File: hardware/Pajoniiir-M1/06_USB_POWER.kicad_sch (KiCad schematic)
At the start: 19 parts

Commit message: hardware: fix local symbol cache keys for ERC
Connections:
- net 5V_SYS: now also U_USB0.4 (EN), U_USB1.4 (EN)
- net GND: now also U_USB0.5 (GND), U_USB1.5 (GND)
- net USB0_FAULT_N: now also U_USB0.1 (OUT)
- net USB0_PWR_EN: now also U_USB0.6 (IN)
- net USB0_SW_OUT: now also U_USB0.3 (FAULT)
- net USB1_FAULT_N: now also U_USB1.1 (OUT)
- net USB1_PWR_EN: now also U_USB1.6 (IN)
- net USB1_SW_OUT: now also U_USB1.3 (FAULT)
- net at R_U_USB0_ILIM.1: now also U_USB0.2 (ILIM)
- net at R_U_USB1_ILIM.1: now also U_USB1.2 (ILIM)
- new net EP/GND: U_USB0.7 (EP/GND), U_USB1.7 (EP/GND)

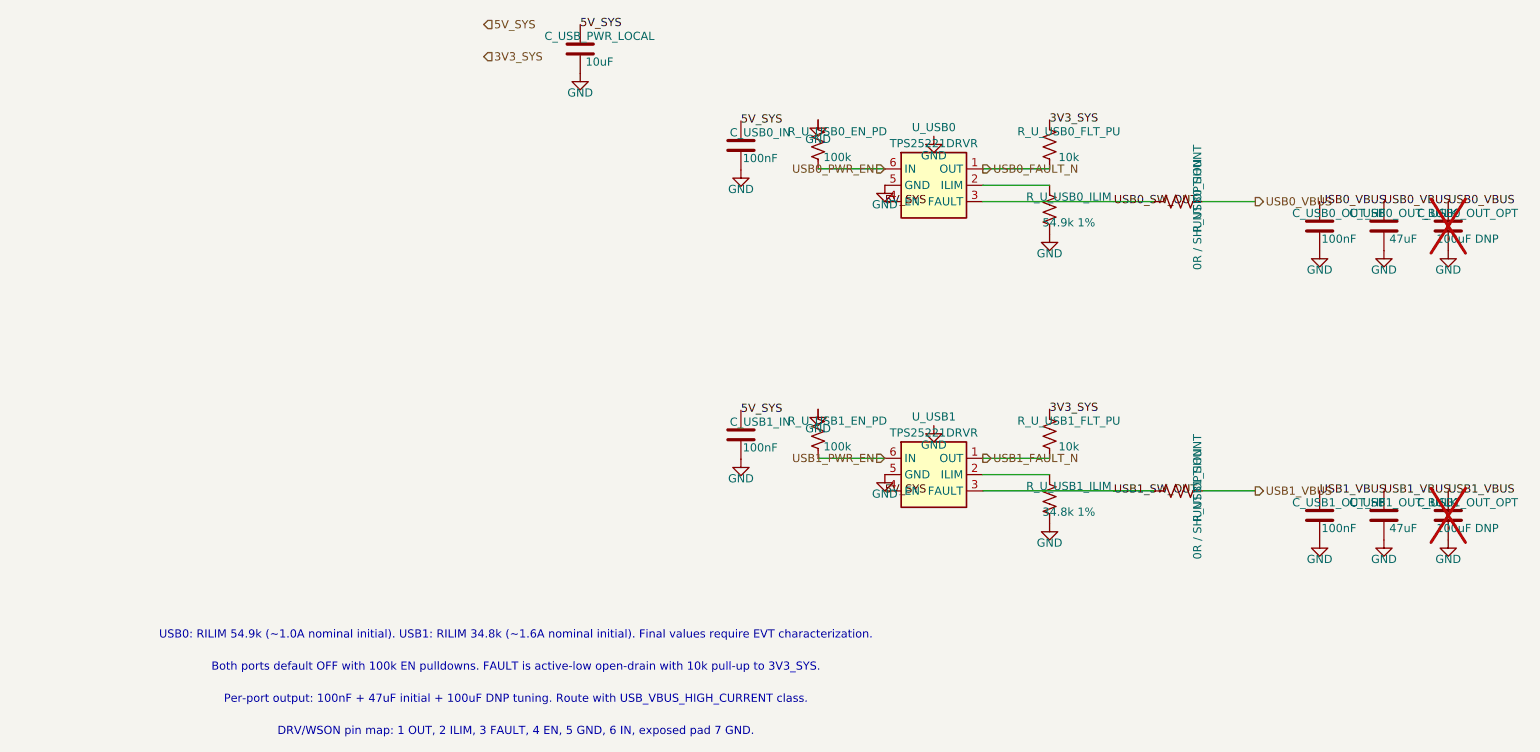
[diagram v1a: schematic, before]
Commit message: hardware: snap child sheets 06-10 to 25 mil grid
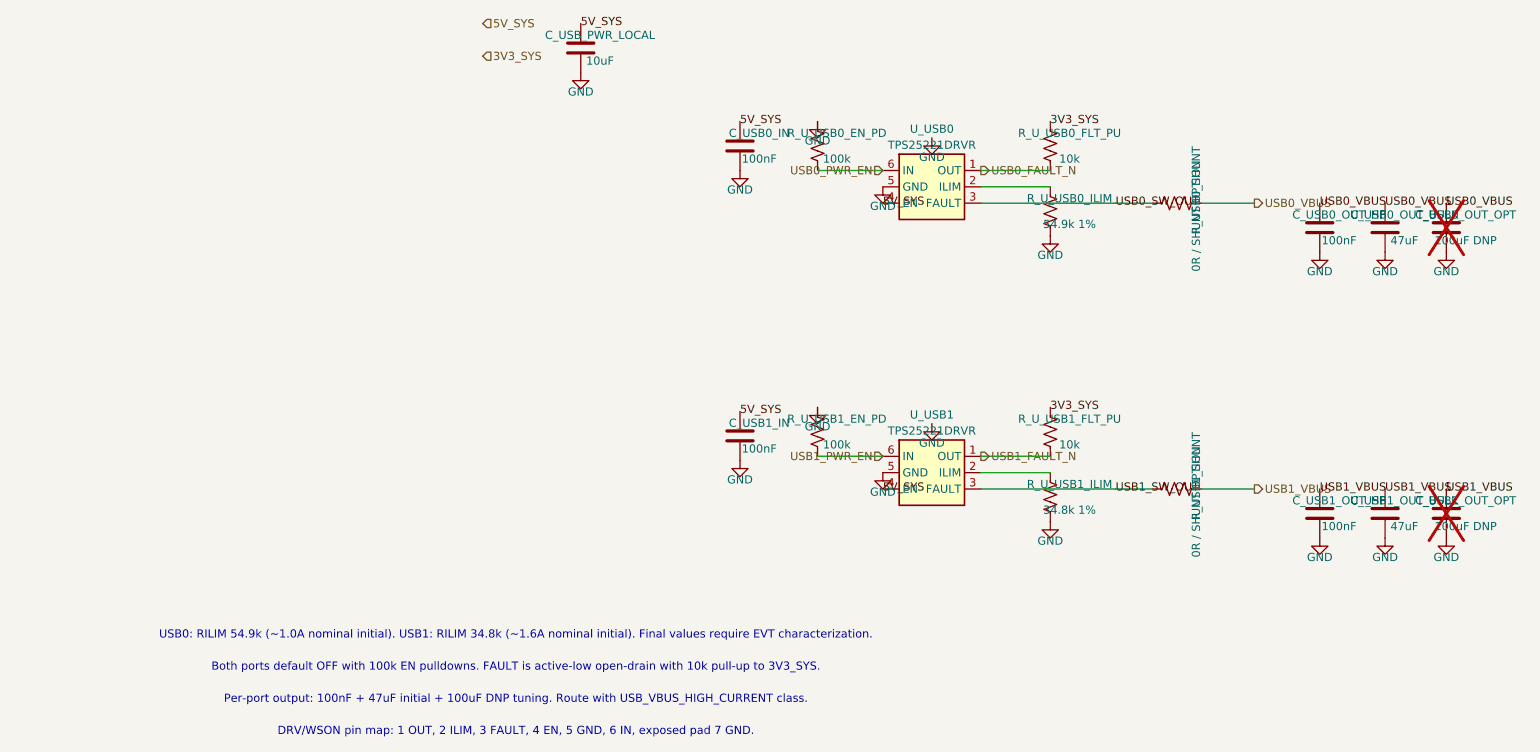
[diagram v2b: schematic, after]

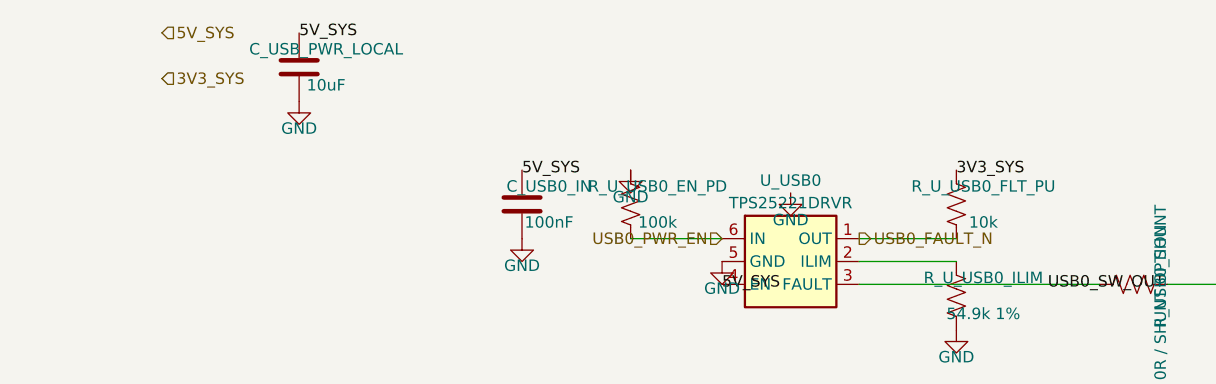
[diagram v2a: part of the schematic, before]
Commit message: hardware: bind core hierarchical ports to nets
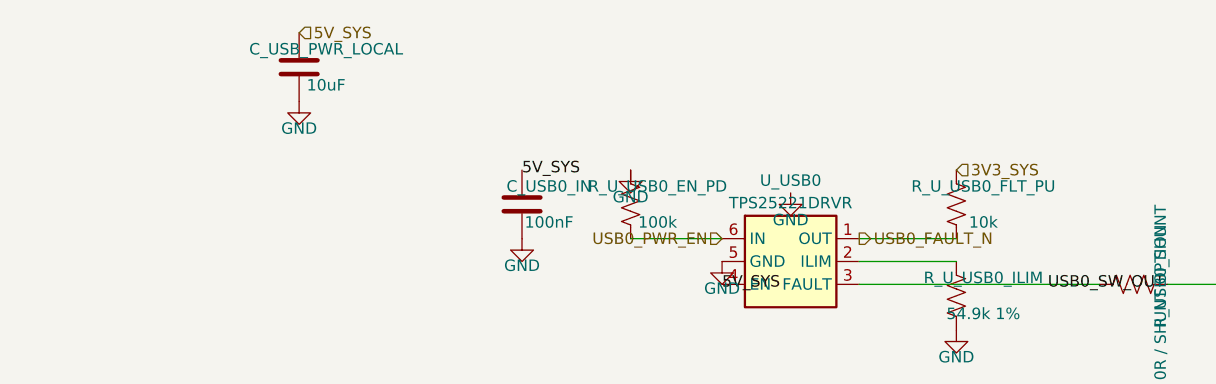
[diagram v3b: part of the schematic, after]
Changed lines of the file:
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@@
     (comment 2 "TPS25221 DRV pinout verified; EP7 grounded")
   )
-  (hierarchical_label "5V_SYS" (shape input) (at 29.845 29.845 0) (effects (font (size 1.27 1.27))))
-  (hierarchical_label "3V3_SYS" (shape input) (at 29.845 34.925 0) (effects (font (size 1.27 1.27))))
+  (hierarchical_label "5V_SYS" (shape input) (at 45.085 29.845 0) (effects (font (size 1.27 1.27))))
+  (hierarchical_label "3V3_SYS" (shape input) (at 118.11 45.085 0) (effects (font (size 1.27 1.27))))
   (symbol
     (lib_id "Device:C") (at 45.085 33.655 0) (unit 1)
@@
     (instances (project "Pajoniiir-M1" (path "/2c8dd352-b7b8-4d9e-8f93-5dd43be2a100/31000006-6b2a-4a3a-8c91-000000000006" (reference "C_USB_PWR_LOCAL") (unit 1))))
   )
-  (label "5V_SYS" (at 45.085 29.845 0) (effects (font (size 1.27 1.27))))
   (symbol
     (lib_id "power:GND") (at 45.085 37.465 0) (unit 1)
@@
     (instances (project "Pajoniiir-M1" (path "/2c8dd352-b7b8-4d9e-8f93-5dd43be2a100/31000006-6b2a-4a3a-8c91-000000000006" (reference "R_U_USB0_FLT_PU") (unit 1))))
   )
-  (label "3V3_SYS" (at 118.11 45.085 0) (effects (font (size 1.27 1.27))))
   (wire (pts (xy 118.11 52.705) (xy 107.315 52.705)) (stroke (width 0) (type default)))
   (symbol

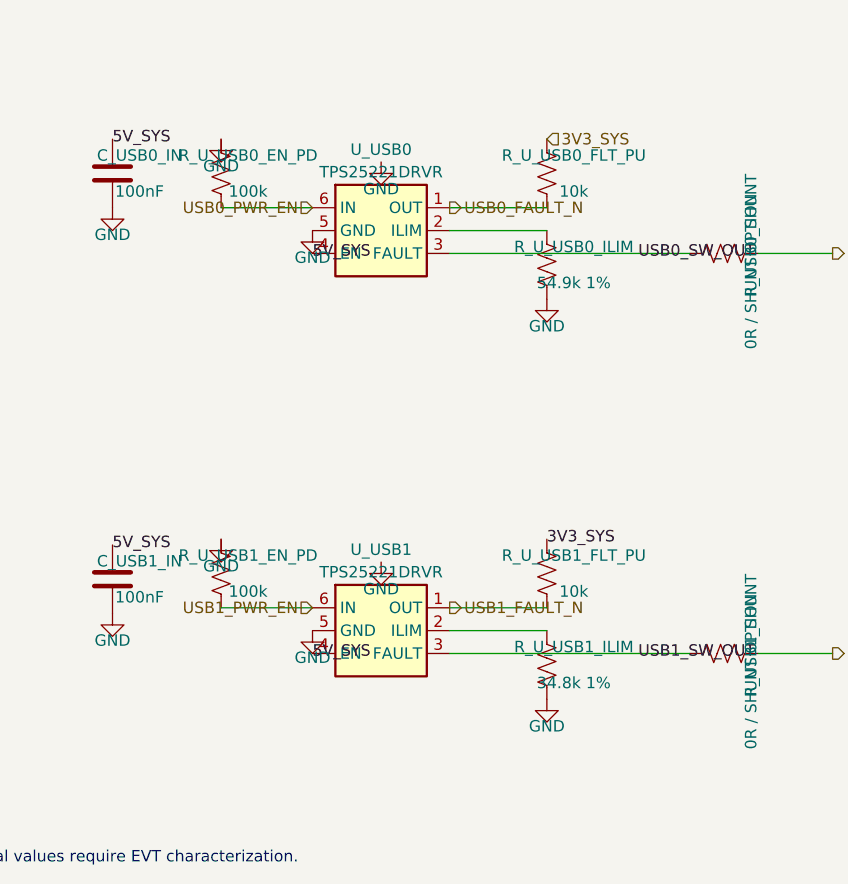
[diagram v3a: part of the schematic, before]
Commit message: hardware: correct dual USB power-switch pin mapping
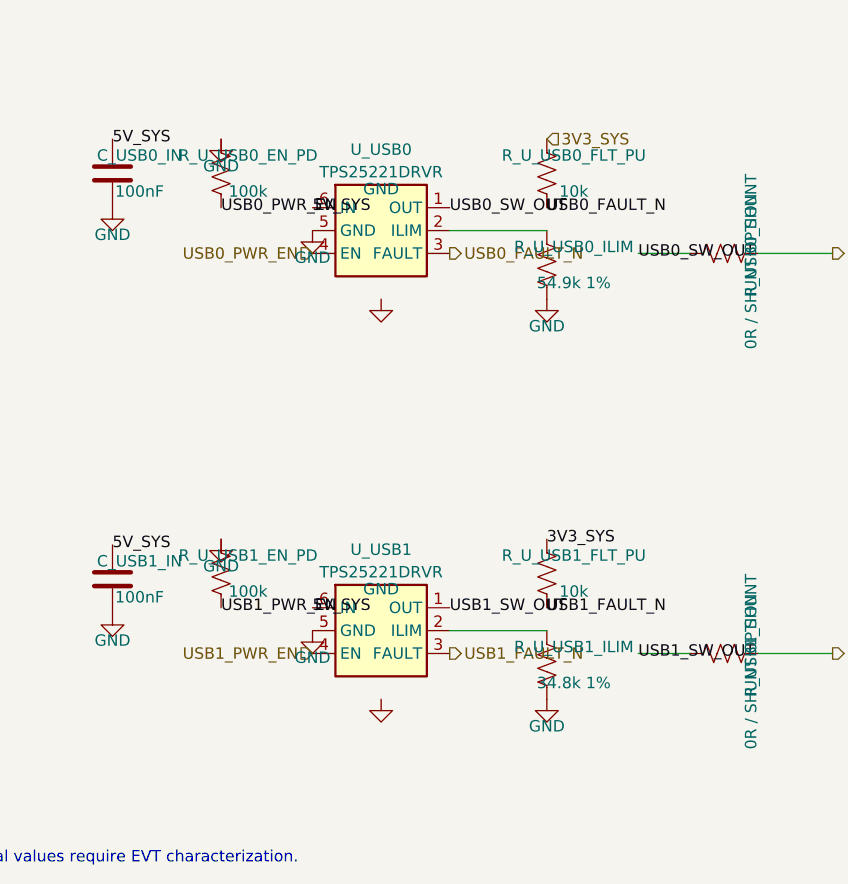
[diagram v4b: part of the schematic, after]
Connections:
- net GND is gone; now on net EP/GND: C_USB0_IN.2, C_USB0_OUT_BULK.2, C_USB0_OUT_HF.2, C_USB0_OUT_OPT.2, C_USB1_IN.2, C_USB1_OUT_BULK.2, C_USB1_OUT_HF.2, C_USB1_OUT_OPT.2, C_USB_PWR_LOCAL.2, R_U_USB0_EN_PD.1, R_U_USB0_ILIM.2, R_U_USB1_EN_PD.1, R_U_USB1_ILIM.2, U_USB0.5 (GND), U_USB1.5 (GND)
- net 5V_SYS: now also U_USB0.6 (IN), U_USB1.6 (IN); no longer U_USB0.4 (EN), U_USB1.4 (EN)
- net USB0_FAULT_N: now also U_USB0.3 (FAULT); no longer U_USB0.1 (OUT)
- net USB0_PWR_EN: now also U_USB0.4 (EN); no longer U_USB0.6 (IN)
- net USB0_SW_OUT: now also U_USB0.1 (OUT); no longer U_USB0.3 (FAULT)
- net USB1_FAULT_N: now also U_USB1.3 (FAULT); no longer U_USB1.1 (OUT)
- net USB1_PWR_EN: now also U_USB1.4 (EN); no longer U_USB1.6 (IN)
- net USB1_SW_OUT: now also U_USB1.1 (OUT); no longer U_USB1.3 (FAULT)
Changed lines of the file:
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@@
     (comment 2 "TPS25221 DRV pinout verified; EP7 grounded")
   )
+  (label "USB0_PWR_EN" (at 81.915 52.705 0) (effects (font (size 1.27 1.27))))
+  (label "USB0_FAULT_N" (at 118.11 52.705 0) (effects (font (size 1.27 1.27))))
+  (label "USB0_SW_OUT" (at 107.315 52.705 0) (effects (font (size 1.27 1.27))))
+  (label "USB1_PWR_EN" (at 81.915 97.155 0) (effects (font (size 1.27 1.27))))
+  (label "USB1_FAULT_N" (at 118.11 97.155 0) (effects (font (size 1.27 1.27))))
+  (label "USB1_SW_OUT" (at 107.315 97.155 0) (effects (font (size 1.27 1.27))))
   (hierarchical_label "5V_SYS" (shape input) (at 45.085 29.845 0) (effects (font (size 1.27 1.27))))
   (hierarchical_label "3V3_SYS" (shape input) (at 118.11 45.085 0) (effects (font (size 1.27 1.27))))
@@
     (instances (project "Pajoniiir-M1" (path "/2c8dd352-b7b8-4d9e-8f93-5dd43be2a100/31000006-6b2a-4a3a-8c91-000000000006" (reference "U_USB0") (unit 1))))
   )
-  (label "5V_SYS" (at 92.075 57.785 0) (effects (font (size 1.27 1.27))))
+  (label "5V_SYS" (at 92.075 52.705 0) (effects (font (size 1.27 1.27))))
   (symbol
     (lib_id "power:GND") (at 92.075 55.245 0) (unit 1)
@@
   )
   (symbol
-    (lib_id "power:GND") (at 99.695 47.625 0) (unit 1)
+    (lib_id "power:GND") (at 99.695 62.865 0) (unit 1)
     (exclude_from_sim no) (in_bom yes) (on_board yes) (dnp no)
     (property "Reference" "#PWR_U_USB0_EP" (at 99.695 53.625 0) (effects (font (size 1.27 1.27)) (hide yes)))
@@
     (instances (project "Pajoniiir-M1" (path "/2c8dd352-b7b8-4d9e-8f93-5dd43be2a100/31000006-6b2a-4a3a-8c91-000000000006" (reference "#PWR_U_USB0_EP") (unit 1))))
   )
-  (hierarchical_label "USB0_PWR_EN" (shape input) (at 92.075 52.705 180) (effects (font (size 1.27 1.27))))
+  (hierarchical_label "USB0_PWR_EN" (shape input) (at 92.075 57.785 180) (effects (font (size 1.27 1.27))))
   (symbol
     (lib_id "Device:R_US") (at 81.915 48.895 0) (unit 1)
@@
     (instances (project "Pajoniiir-M1" (path "/2c8dd352-b7b8-4d9e-8f93-5dd43be2a100/31000006-6b2a-4a3a-8c91-000000000006" (reference "R_U_USB0_EN_PD") (unit 1))))
   )
-  (wire (pts (xy 81.915 52.705) (xy 92.075 52.705)) (stroke (width 0) (type default)))
   (symbol
     (lib_id "power:GND") (at 81.915 45.085 0) (unit 1)
@@
     (instances (project "Pajoniiir-M1" (path "/2c8dd352-b7b8-4d9e-8f93-5dd43be2a100/31000006-6b2a-4a3a-8c91-000000000006" (reference "#PWR_U_USB0_EN") (unit 1))))
   )
-  (hierarchical_label "USB0_FAULT_N" (shape output) (at 107.315 52.705 0) (effects (font (size 1.27 1.27))))
+  (hierarchical_label "USB0_FAULT_N" (shape output) (at 107.315 57.785 0) (effects (font (size 1.27 1.27))))
   (symbol
     (lib_id "Device:R_US") (at 118.11 48.895 0) (unit 1)
@@
     (instances (project "Pajoniiir-M1" (path "/2c8dd352-b7b8-4d9e-8f93-5dd43be2a100/31000006-6b2a-4a3a-8c91-000000000006" (reference "R_U_USB0_FLT_PU") (unit 1))))
   )
-  (wire (pts (xy 118.11 52.705) (xy 107.315 52.705)) (stroke (width 0) (type default)))
   (symbol
     (lib_id "Device:R_US") (at 118.11 59.055 0) (unit 1)
@@
     (instances (project "Pajoniiir-M1" (path "/2c8dd352-b7b8-4d9e-8f93-5dd43be2a100/31000006-6b2a-4a3a-8c91-000000000006" (reference "#PWR_U_USB0_ILIM") (unit 1))))
   )
-  (wire (pts (xy 107.315 57.785) (xy 128.27 57.785)) (stroke (width 0) (type default)))
   (label "USB0_SW_OUT" (at 128.27 57.785 0) (effects (font (size 1.27 1.27))))
   (symbol
@@
     (instances (project "Pajoniiir-M1" (path "/2c8dd352-b7b8-4d9e-8f93-5dd43be2a100/31000006-6b2a-4a3a-8c91-000000000006" (reference "U_USB1") (unit 1))))
   )
-  (label "5V_SYS" (at 92.075 102.235 0) (effects (font (size 1.27 1.27))))
+  (label "5V_SYS" (at 92.075 97.155 0) (effects (font (size 1.27 1.27))))
   (symbol
     (lib_id "power:GND") (at 92.075 99.695 0) (unit 1)
@@
   )
   (symbol
-    (lib_id "power:GND") (at 99.695 92.075 0) (unit 1)
+    (lib_id "power:GND") (at 99.695 107.315 0) (unit 1)
     (exclude_from_sim no) (in_bom yes) (on_board yes) (dnp no)
     (property "Reference" "#PWR_U_USB1_EP" (at 99.695 98.075 0) (effects (font (size 1.27 1.27)) (hide yes)))
@@
     (instances (project "Pajoniiir-M1" (path "/2c8dd352-b7b8-4d9e-8f93-5dd43be2a100/31000006-6b2a-4a3a-8c91-000000000006" (reference "#PWR_U_USB1_EP") (unit 1))))
   )
-  (hierarchical_label "USB1_PWR_EN" (shape input) (at 92.075 97.155 180) (effects (font (size 1.27 1.27))))
+  (hierarchical_label "USB1_PWR_EN" (shape input) (at 92.075 102.235 180) (effects (font (size 1.27 1.27))))
   (symbol
     (lib_id "Device:R_US") (at 81.915 93.345 0) (unit 1)
@@
     (instances (project "Pajoniiir-M1" (path "/2c8dd352-b7b8-4d9e-8f93-5dd43be2a100/31000006-6b2a-4a3a-8c91-000000000006" (reference "R_U_USB1_EN_PD") (unit 1))))
   )
-  (wire (pts (xy 81.915 97.155) (xy 92.075 97.155)) (stroke (width 0) (type default)))
   (symbol
     (lib_id "power:GND") (at 81.915 89.535 0) (unit 1)
@@
     (instances (project "Pajoniiir-M1" (path "/2c8dd352-b7b8-4d9e-8f93-5dd43be2a100/31000006-6b2a-4a3a-8c91-000000000006" (reference "#PWR_U_USB1_EN") (unit 1))))
   )
-  (hierarchical_label "USB1_FAULT_N" (shape output) (at 107.315 97.155 0) (effects (font (size 1.27 1.27))))
+  (hierarchical_label "USB1_FAULT_N" (shape output) (at 107.315 102.235 0) (effects (font (size 1.27 1.27))))
   (symbol
     (lib_id "Device:R_US") (at 118.11 93.345 0) (unit 1)
@@
   )
   (label "3V3_SYS" (at 118.11 89.535 0) (effects (font (size 1.27 1.27))))
-  (wire (pts (xy 118.11 97.155) (xy 107.315 97.155)) (stroke (width 0) (type default)))
   (symbol
     (lib_id "Device:R_US") (at 118.11 103.505 0) (unit 1)
@@
     (instances (project "Pajoniiir-M1" (path "/2c8dd352-b7b8-4d9e-8f93-5dd43be2a100/31000006-6b2a-4a3a-8c91-000000000006" (reference "#PWR_U_USB1_ILIM") (unit 1))))
   )
-  (wire (pts (xy 107.315 102.235) (xy 128.27 102.235)) (stroke (width 0) (type default)))
   (label "USB1_SW_OUT" (at 128.27 102.235 0) (effects (font (size 1.27 1.27))))
   (symbol
